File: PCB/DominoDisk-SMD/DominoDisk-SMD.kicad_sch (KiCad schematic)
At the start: 26 parts, among them J1 Daisy port out, J2 ICSP_ISP6, J3 Daisy port in, J4 UART, K1 TF-104 MicroSD card holder, U1 PC817C-S, U2 ATmega328P-AU, U3 TXB0104PWR level shifter, U4 SE5218 voltage regulator, Y1 CSTNE16M0V530000R0 Resonator

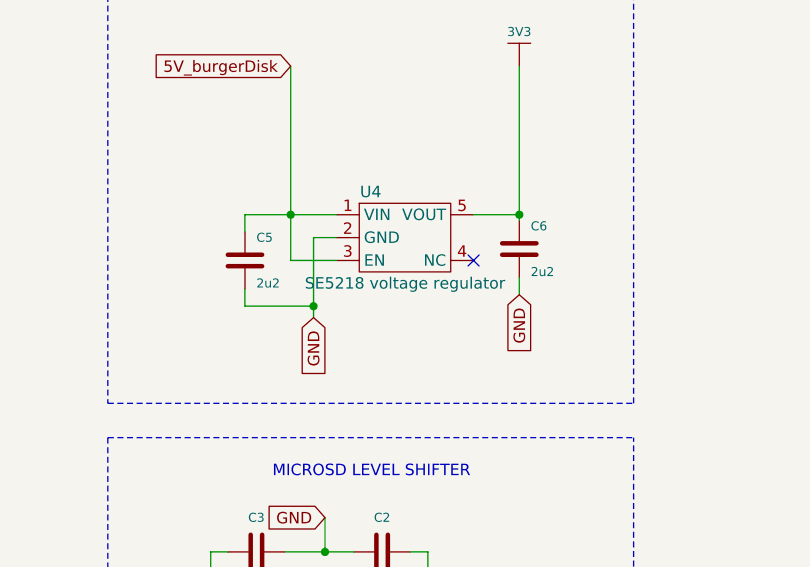
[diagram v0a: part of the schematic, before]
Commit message: Move logo out of PCB
until I'm sure Rebecca's estate is OK with it
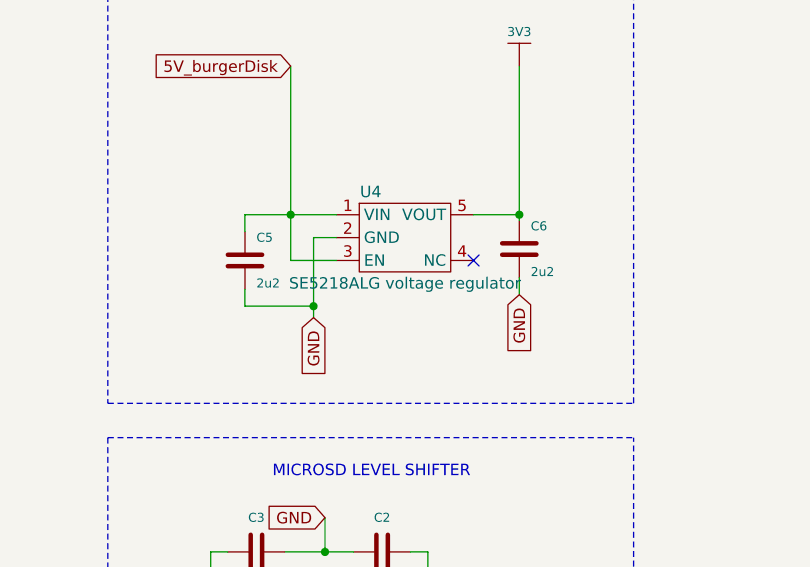
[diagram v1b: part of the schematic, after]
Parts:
- U4: value SE5218 voltage regulator -> SE5218ALG voltage regulator
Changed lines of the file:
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@@
 			)
 		)
-		(property "Value" "SE5218 voltage regulator"
+		(property "Value" "SE5218ALG voltage regulator"
 			(at 255.27 93.345 0)
 			(effects

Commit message: Switch some parts to Basic
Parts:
- C2, C3, C4: LCSC C1590 -> C14663
- R1: LCSC C22369795 -> C22775
- R3, R4, R6: LCSC C177337 -> C25804
- R5: LCSC C177343 -> C21190
- R7: LCSC C177341 -> C23138
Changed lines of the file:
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@@
 			)
 		)
-		(property "LCSC" "C1590"
+		(property "LCSC" "C14663"
 			(at 238.76 123.19 0)
 			(effects
@@
 			)
 		)
-		(property "LCSC" " C1590"
+		(property "LCSC" "C14663"
 			(at 29.21 118.11 90)
 			(effects
@@
 			)
 		)
-		(property "LCSC" "C177337"
+		(property "LCSC" "C25804"
 			(at 101.6 76.2 0)
 			(effects
@@
 			)
 		)
-		(property "LCSC" "C177337"
+		(property "LCSC" "C25804"
 			(at 256.54 152.4 90)
 			(effects
@@
 			)
 		)
-		(property "LCSC" " C177337"
+		(property "LCSC" "C25804"
 			(at 106.68 146.05 0)
 			(effects
@@
 			)
 		)
-		(property "LCSC" "C22369795"
+		(property "LCSC" "C22775"
 			(at 114.3 158.75 0)
 			(effects
@@
 			)
 		)
-		(property "LCSC" "C177341"
+		(property "LCSC" "C23138"
 			(at 60.96 55.88 0)
 			(effects
@@
 			)
 		)
-		(property "LCSC" "C1590"
+		(property "LCSC" "C14663"
 			(at 252.73 123.19 0)
 			(effects
@@
 			)
 		)
-		(property "LCSC" "C177343"
+		(property "LCSC" "C21190"
 			(at 101.6 71.12 0)
 			(effects

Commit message: Move to bigger pads for diodes
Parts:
- D3: footprint Diode_SMD:D_SOD-323F -> Diode_SMD:D_SOD-323_HandSoldering
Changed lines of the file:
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@@
 			)
 		)
-		(property "Footprint" "Diode_SMD:D_SOD-323F"
+		(property "Footprint" "Diode_SMD:D_SOD-323_HandSoldering"
 			(at 54.61 69.215 0)
 			(effects
